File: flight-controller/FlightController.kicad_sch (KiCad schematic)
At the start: 31 parts, among them J1 MSD-4-A, J2 Conn_01x03_Pin, J3 Conn_01x03_Pin, J4 Conn_01x03_Pin, J5 Conn_01x03_Pin, J6 USB4215-03-A_REVA, J7 Conn_01x03_Pin, J8 Conn_01x03_Pin, J9 Conn_01x04_Pin, U1 ESP32-S3-WROOM-1, U2 TPS629210DRLR, U3 MMC5983MA, U4 BMI270, U5 BMP581

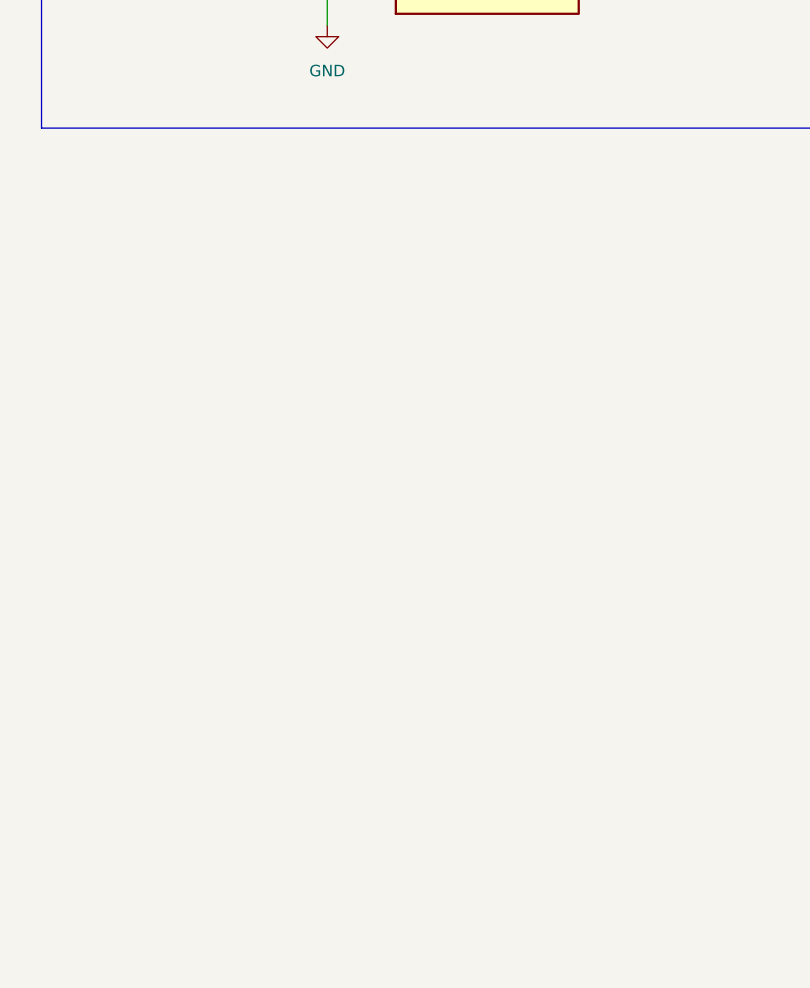
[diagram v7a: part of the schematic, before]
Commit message: add mounting holes
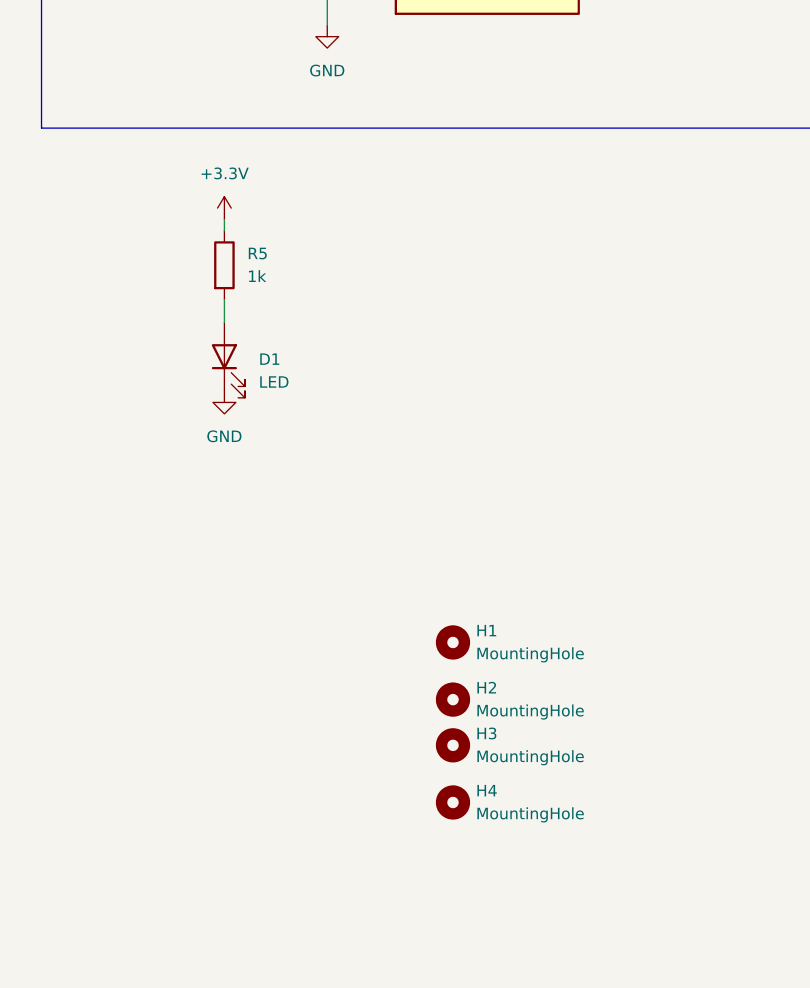
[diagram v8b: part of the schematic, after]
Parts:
- added D1: LED, LED_SMD:LED_0805_2012Metric, symbol Device:LED
- added H1, H2, H3, H4: MountingHole, MountingHole:MountingHole_3.2mm_M3, symbol Mechanical:MountingHole
- added R5: 1k, Resistor_SMD:R_0603_1608Metric_Pad0.98x0.95mm_HandSolder, symbol Device:R
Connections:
- net +3.3V: now also R5.1
- net GND: now also D1.1 (K)
- new net: D1.2 (A), R5.2
